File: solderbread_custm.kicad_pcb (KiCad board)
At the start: 2 copper layers, 830 parts, among them J1 Conn_01x01, J10 Conn_01x01 J, J100 Conn_01x01 J, J101 Conn_01x01 A, J102 Conn_01x01 B, J103 Conn_01x01 C, J104 Conn_01x01 D, J105 Conn_01x01 E, J106 Conn_01x01 F, J107 Conn_01x01 G, J108 Conn_01x01 H, J109 Conn_01x01 I, J11 Conn_01x01 A, J110 Conn_01x01 J, J111 Conn_01x01 A, J112 Conn_01x01 B, J113 Conn_01x01 C, J114 Conn_01x01 D, J115 Conn_01x01 E, J116 Conn_01x01 F, J117 Conn_01x01 G, J118 Conn_01x01 H, J119 Conn_01x01 I, J12 Conn_01x01 B, J120 Conn_01x01 J, J121 Conn_01x01 A, J122 Conn_01x01 B, J123 Conn_01x01 C, J124 Conn_01x01 D, J125 Conn_01x01 E, J126 Conn_01x01 F, J127 Conn_01x01 G, J128 Conn_01x01 H, J129 Conn_01x01 I, J13 Conn_01x01 C, J130 Conn_01x01 J, J131 Conn_01x01 A, J132 Conn_01x01 B, J133 Conn_01x01 C, J134 Conn_01x01 D, J135 Conn_01x01 E, J136 Conn_01x01 F, J137 Conn_01x01 G, J138 Conn_01x01 H, J139 Conn_01x01 I, J14 Conn_01x01 D, J140 Conn_01x01 J, J141 Conn_01x01 A, J142 Conn_01x01 B, J143 Conn_01x01 C, J144 Conn_01x01 D, J145 Conn_01x01 E, J146 Conn_01x01 F, J147 Conn_01x01 G, J148 Conn_01x01 H, J149 Conn_01x01 I, J15 Conn_01x01 E, J150 Conn_01x01 J, J151 Conn_01x01 A, J152 Conn_01x01 B, J153 Conn_01x01 C, J154 Conn_01x01 D, J155 Conn_01x01 E, J156 Conn_01x01 F, J157 Conn_01x01 G, J158 Conn_01x01 H, J159 Conn_01x01 I, J16 Conn_01x01 F, J160 Conn_01x01 J, J161 Conn_01x01 A, J162 Conn_01x01 B, J163 Conn_01x01 C, J164 Conn_01x01 D, J165 Conn_01x01 E, J166 Conn_01x01 F, J167 Conn_01x01 G, J168 Conn_01x01 H, J169 Conn_01x01 I, J17 Conn_01x01 G, J170 Conn_01x01 J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

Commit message: [ADD] Basic Pin rows in pcb
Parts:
- moved J591 193.5 mm to (243.8, 96.5)
- moved J592 193.5 mm to (243.8, 99.1)
- moved J593 193.5 mm to (243.8, 101.6)
- moved J594 193.5 mm to (243.8, 104.1)
- moved J595 193.5 mm to (243.8, 106.7)
- moved J596 192.4 mm to (243.8, 114.3)
- moved J597 192.4 mm to (243.8, 116.8)
- moved J598 192.4 mm to (243.8, 119.4)
- moved J599 192.4 mm to (243.8, 121.9)
- moved J600 192.3 mm to (243.8, 124.5)
- moved J625 190.1 mm to (251.5, 106.7)
- moved J624 190.1 mm to (251.5, 104.1)
- moved J623 190.0 mm to (251.5, 101.6)
- moved J622 190.0 mm to (251.5, 99.1)
- moved J621 190.0 mm to (251.5, 96.5)
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
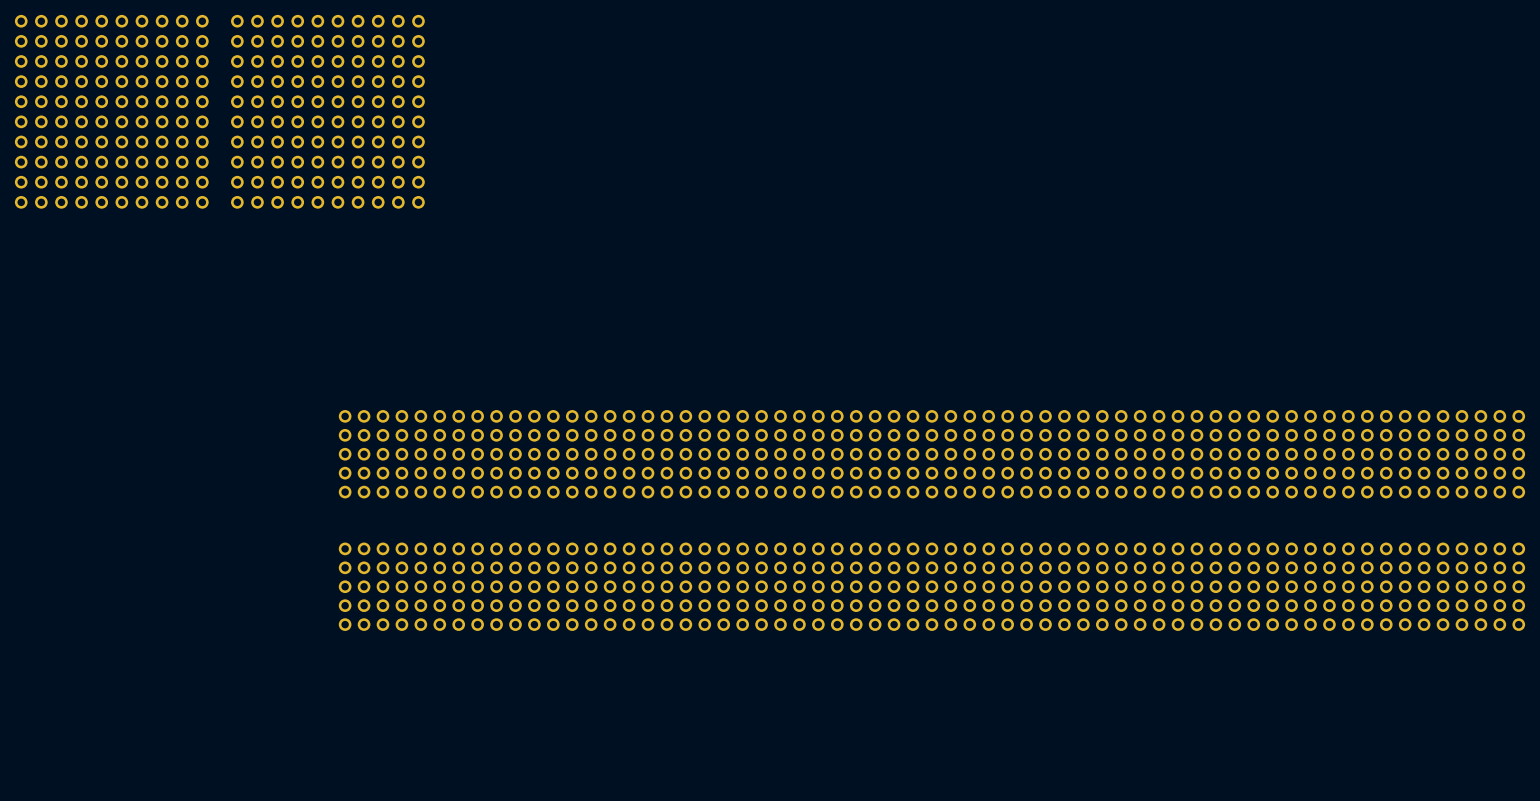
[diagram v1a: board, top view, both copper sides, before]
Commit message: [ADD] footprints placed
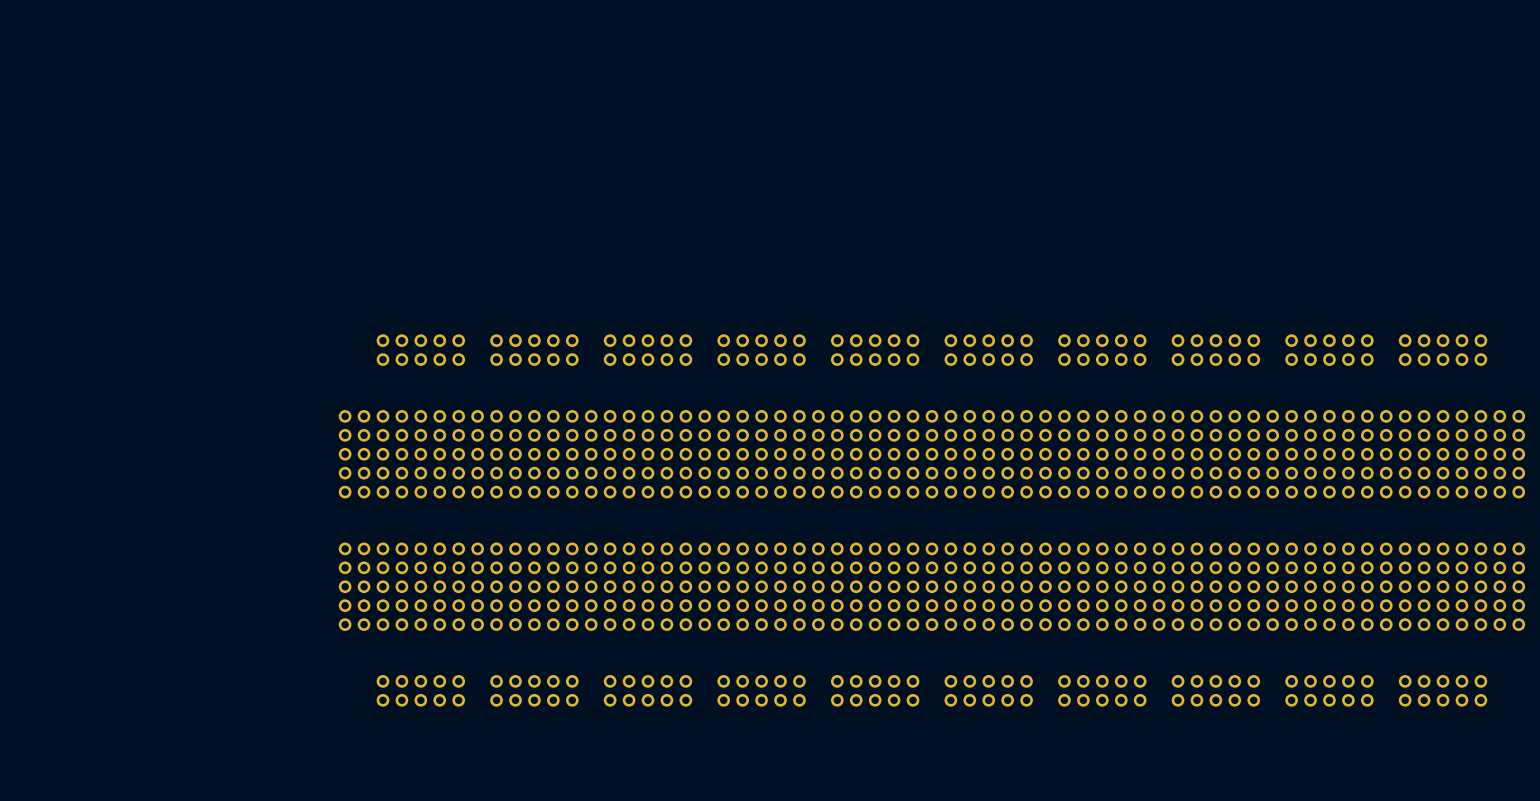
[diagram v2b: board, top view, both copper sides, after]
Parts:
- moved J735 188.0 mm to (236.2, 86.4)
- moved J745 187.8 mm to (238.8, 86.4)
- moved J755 187.7 mm to (241.3, 86.4)
- moved J765 187.5 mm to (243.8, 86.4)
- moved J775 187.4 mm to (246.4, 86.4)
- moved J780 178.1 mm to (236.2, 88.9)
- moved J790 177.9 mm to (238.8, 88.9)
- moved J800 177.8 mm to (241.3, 88.9)
- moved J810 177.6 mm to (243.8, 88.9)
- moved J820 177.5 mm to (246.4, 88.9)
- moved J665 175.7 mm to (243.8, 134.6)
- moved J675 175.5 mm to (246.4, 134.6)
- moved J736 172.5 mm to (221.0, 86.4)
- moved J746 172.4 mm to (223.5, 86.4)
- moved J756 172.2 mm to (226.1, 86.4)
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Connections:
- J656 pad 1: Net-(J631-Pin_1) -> Net-(J656-Pin_1)
- J657 pad 1: Net-(J631-Pin_1) -> Net-(J656-Pin_1)
- J658 pad 1: Net-(J631-Pin_1) -> Net-(J656-Pin_1)
- J659 pad 1: Net-(J631-Pin_1) -> Net-(J656-Pin_1)
- J660 pad 1: Net-(J631-Pin_1) -> Net-(J656-Pin_1)
- J661 pad 1: Net-(J631-Pin_1) -> Net-(J656-Pin_1)
- J662 pad 1: Net-(J631-Pin_1) -> Net-(J656-Pin_1)
- J663 pad 1: Net-(J631-Pin_1) -> Net-(J656-Pin_1)
- J664 pad 1: Net-(J631-Pin_1) -> Net-(J656-Pin_1)
- J665 pad 1: Net-(J631-Pin_1) -> Net-(J656-Pin_1)
- J666 pad 1: Net-(J631-Pin_1) -> Net-(J656-Pin_1)
- J667 pad 1: Net-(J631-Pin_1) -> Net-(J656-Pin_1)
- J668 pad 1: Net-(J631-Pin_1) -> Net-(J656-Pin_1)
- J669 pad 1: Net-(J631-Pin_1) -> Net-(J656-Pin_1)
- J670 pad 1: Net-(J631-Pin_1) -> Net-(J656-Pin_1)
- J671 pad 1: Net-(J631-Pin_1) -> Net-(J656-Pin_1)
- J672 pad 1: Net-(J631-Pin_1) -> Net-(J656-Pin_1)
- J673 pad 1: Net-(J631-Pin_1) -> Net-(J656-Pin_1)
- J674 pad 1: Net-(J631-Pin_1) -> Net-(J656-Pin_1)
- J675 pad 1: Net-(J631-Pin_1) -> Net-(J656-Pin_1)
- J676 pad 1: Net-(J631-Pin_1) -> Net-(J656-Pin_1)
- J677 pad 1: Net-(J631-Pin_1) -> Net-(J656-Pin_1)
- J678 pad 1: Net-(J631-Pin_1) -> Net-(J656-Pin_1)
- J679 pad 1: Net-(J631-Pin_1) -> Net-(J656-Pin_1)
- J680 pad 1: Net-(J631-Pin_1) -> Net-(J656-Pin_1)
- J706 pad 1: Net-(J681-Pin_1) -> Net-(J706-Pin_1)
- J707 pad 1: Net-(J681-Pin_1) -> Net-(J706-Pin_1)
- J708 pad 1: Net-(J681-Pin_1) -> Net-(J706-Pin_1)
- J709 pad 1: Net-(J681-Pin_1) -> Net-(J706-Pin_1)
- J710 pad 1: Net-(J681-Pin_1) -> Net-(J706-Pin_1)
- J711 pad 1: Net-(J681-Pin_1) -> Net-(J706-Pin_1)
- J712 pad 1: Net-(J681-Pin_1) -> Net-(J706-Pin_1)
- J713 pad 1: Net-(J681-Pin_1) -> Net-(J706-Pin_1)
- J714 pad 1: Net-(J681-Pin_1) -> Net-(J706-Pin_1)
- J715 pad 1: Net-(J681-Pin_1) -> Net-(J706-Pin_1)
- J716 pad 1: Net-(J681-Pin_1) -> Net-(J706-Pin_1)
- J717 pad 1: Net-(J681-Pin_1) -> Net-(J706-Pin_1)
- J718 pad 1: Net-(J681-Pin_1) -> Net-(J706-Pin_1)
- J719 pad 1: Net-(J681-Pin_1) -> Net-(J706-Pin_1)
- J720 pad 1: Net-(J681-Pin_1) -> Net-(J706-Pin_1)
- J721 pad 1: Net-(J681-Pin_1) -> Net-(J706-Pin_1)
- J722 pad 1: Net-(J681-Pin_1) -> Net-(J706-Pin_1)
- J723 pad 1: Net-(J681-Pin_1) -> Net-(J706-Pin_1)
- J724 pad 1: Net-(J681-Pin_1) -> Net-(J706-Pin_1)
- J725 pad 1: Net-(J681-Pin_1) -> Net-(J706-Pin_1)
- J726 pad 1: Net-(J681-Pin_1) -> Net-(J706-Pin_1)
- J727 pad 1: Net-(J681-Pin_1) -> Net-(J706-Pin_1)
- J728 pad 1: Net-(J681-Pin_1) -> Net-(J706-Pin_1)
- J729 pad 1: Net-(J681-Pin_1) -> Net-(J706-Pin_1)
- J730 pad 1: Net-(J681-Pin_1) -> Net-(J706-Pin_1)
- J780 pad 1: Net-(J1-Pin_1) -> Net-(J780-Pin_1)
- J781 pad 1: Net-(J1-Pin_1) -> Net-(J780-Pin_1)
- J782 pad 1: Net-(J1-Pin_1) -> Net-(J780-Pin_1)
- J783 pad 1: Net-(J1-Pin_1) -> Net-(J780-Pin_1)
- J784 pad 1: Net-(J1-Pin_1) -> Net-(J780-Pin_1)
- J785 pad 1: Net-(J735-Pin_1) -> Net-(J785-Pin_1)
- J786 pad 1: Net-(J735-Pin_1) -> Net-(J785-Pin_1)
- J787 pad 1: Net-(J735-Pin_1) -> Net-(J785-Pin_1)
- J788 pad 1: Net-(J735-Pin_1) -> Net-(J785-Pin_1)
- J789 pad 1: Net-(J735-Pin_1) -> Net-(J785-Pin_1)
- J790 pad 1: Net-(J1-Pin_1) -> Net-(J780-Pin_1)
- J791 pad 1: Net-(J1-Pin_1) -> Net-(J780-Pin_1)
- J792 pad 1: Net-(J1-Pin_1) -> Net-(J780-Pin_1)
- J793 pad 1: Net-(J1-Pin_1) -> Net-(J780-Pin_1)
- J794 pad 1: Net-(J1-Pin_1) -> Net-(J780-Pin_1)
- J795 pad 1: Net-(J735-Pin_1) -> Net-(J785-Pin_1)
- J796 pad 1: Net-(J735-Pin_1) -> Net-(J785-Pin_1)
- J797 pad 1: Net-(J735-Pin_1) -> Net-(J785-Pin_1)
- J798 pad 1: Net-(J735-Pin_1) -> Net-(J785-Pin_1)
- J799 pad 1: Net-(J735-Pin_1) -> Net-(J785-Pin_1)
- J800 pad 1: Net-(J1-Pin_1) -> Net-(J780-Pin_1)
- J801 pad 1: Net-(J1-Pin_1) -> Net-(J780-Pin_1)
- J802 pad 1: Net-(J1-Pin_1) -> Net-(J780-Pin_1)
- J803 pad 1: Net-(J1-Pin_1) -> Net-(J780-Pin_1)
- J804 pad 1: Net-(J1-Pin_1) -> Net-(J780-Pin_1)
- J805 pad 1: Net-(J735-Pin_1) -> Net-(J785-Pin_1)
- J806 pad 1: Net-(J735-Pin_1) -> Net-(J785-Pin_1)
- J807 pad 1: Net-(J735-Pin_1) -> Net-(J785-Pin_1)
- J808 pad 1: Net-(J735-Pin_1) -> Net-(J785-Pin_1)
- J809 pad 1: Net-(J735-Pin_1) -> Net-(J785-Pin_1)
- J810 pad 1: Net-(J1-Pin_1) -> Net-(J780-Pin_1)
- J811 pad 1: Net-(J1-Pin_1) -> Net-(J780-Pin_1)
- J812 pad 1: Net-(J1-Pin_1) -> Net-(J780-Pin_1)
- J813 pad 1: Net-(J1-Pin_1) -> Net-(J780-Pin_1)
- J814 pad 1: Net-(J1-Pin_1) -> Net-(J780-Pin_1)
- J815 pad 1: Net-(J735-Pin_1) -> Net-(J785-Pin_1)
- J816 pad 1: Net-(J735-Pin_1) -> Net-(J785-Pin_1)
- J817 pad 1: Net-(J735-Pin_1) -> Net-(J785-Pin_1)
- J818 pad 1: Net-(J735-Pin_1) -> Net-(J785-Pin_1)
- J819 pad 1: Net-(J735-Pin_1) -> Net-(J785-Pin_1)
- J820 pad 1: Net-(J1-Pin_1) -> Net-(J780-Pin_1)
- J821 pad 1: Net-(J1-Pin_1) -> Net-(J780-Pin_1)
- J822 pad 1: Net-(J1-Pin_1) -> Net-(J780-Pin_1)
- J823 pad 1: Net-(J1-Pin_1) -> Net-(J780-Pin_1)
- J824 pad 1: Net-(J1-Pin_1) -> Net-(J780-Pin_1)
- J825 pad 1: Net-(J735-Pin_1) -> Net-(J785-Pin_1)
- J826 pad 1: Net-(J735-Pin_1) -> Net-(J785-Pin_1)
- J827 pad 1: Net-(J735-Pin_1) -> Net-(J785-Pin_1)
- J828 pad 1: Net-(J735-Pin_1) -> Net-(J785-Pin_1)
- J829 pad 1: Net-(J735-Pin_1) -> Net-(J785-Pin_1)

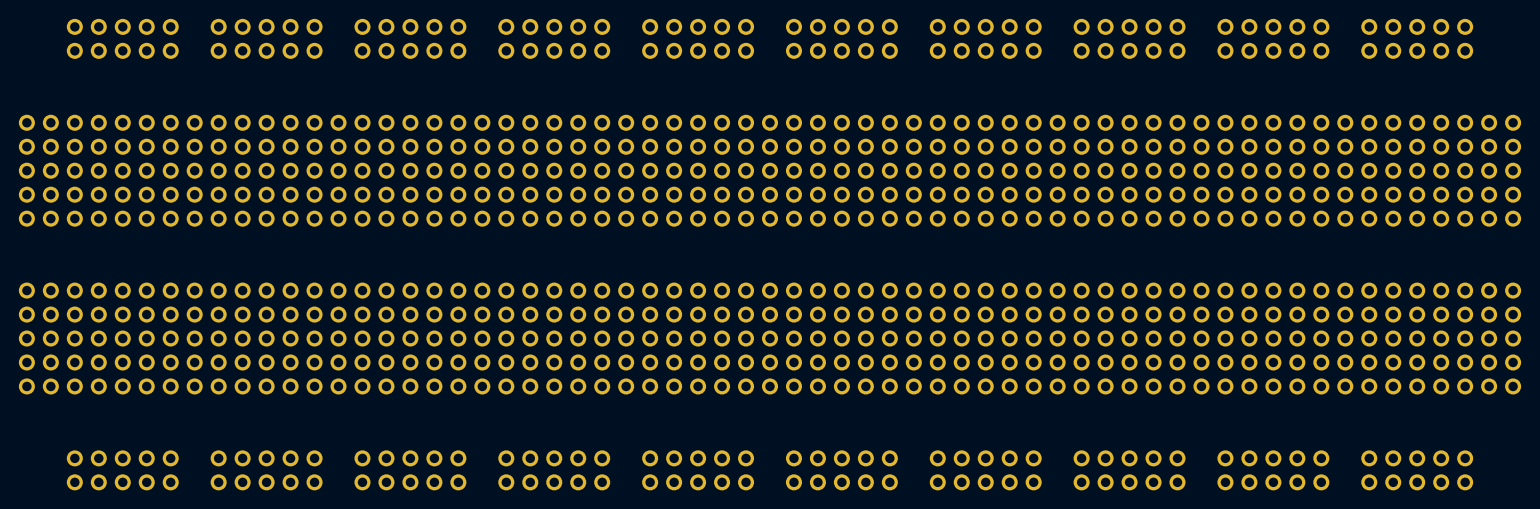
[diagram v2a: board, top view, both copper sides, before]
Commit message: [ADD] Teardrops on top layer
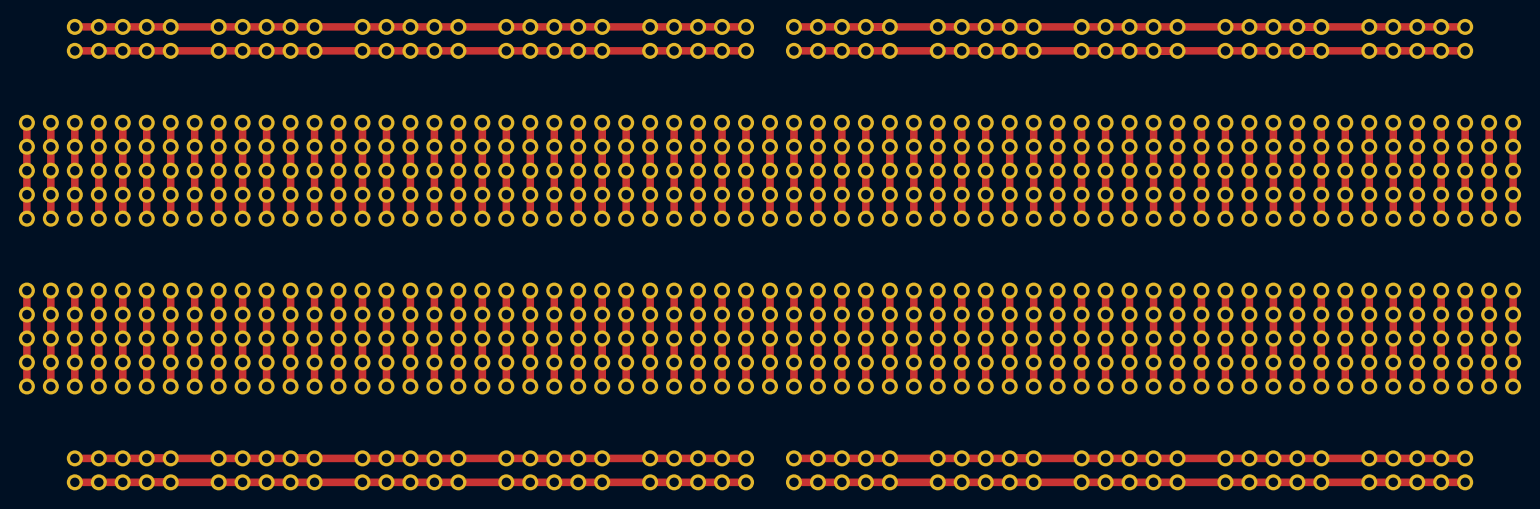
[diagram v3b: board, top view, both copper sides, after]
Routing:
- net Net-(J780-Pin_1): track 0.00 -> 76.2 mm
- net Net-(J735-Pin_1): track 0.00 -> 76.2 mm
- net Net-(J706-Pin_1): track 0.00 -> 76.2 mm
- net Net-(J681-Pin_1): track 0.00 -> 73.7 mm
- net Net-(J631-Pin_1): track 0.00 -> 73.7 mm
- net Net-(J785-Pin_1): track 0.00 -> 71.1 mm
- net Net-(J656-Pin_1): track 0.00 -> 71.1 mm
- net Net-(J1-Pin_1): track 0.00 -> 71.1 mm
- net Net-(J91-Pin_1): track 0.00 -> 10.2 mm
- net Net-(J81-Pin_1): track 0.00 -> 10.2 mm
- net Net-(J71-Pin_1): track 0.00 -> 10.2 mm
- net Net-(J621-Pin_1): track 0.00 -> 10.2 mm
- net Net-(J611-Pin_1): track 0.00 -> 10.2 mm
- net Net-(J61-Pin_1): track 0.00 -> 10.2 mm
- net Net-(J601-Pin_1): track 0.00 -> 10.2 mm
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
